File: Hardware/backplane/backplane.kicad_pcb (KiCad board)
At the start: 2 copper layers, 99.9 x 99.9 mm, 56 parts, among them J1 USB_B_Micro, SW1 SW_SPST, U2 MAX811SEUS-T, U3 MAX811SEUS-T, U4 PAL24, X1 CXO_DIP8

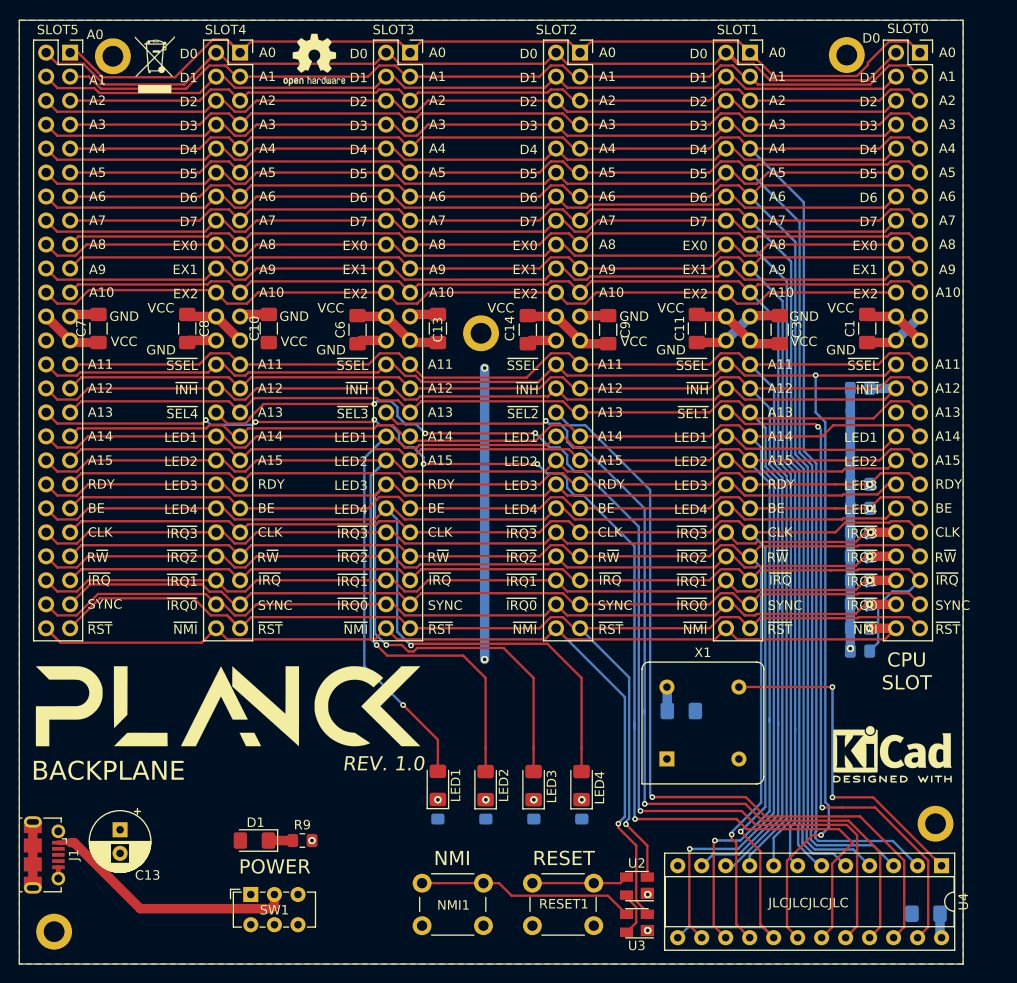
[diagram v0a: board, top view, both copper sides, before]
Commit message: Each slot has an individual interrupt line, to prevent two cards using the same interrupt line.
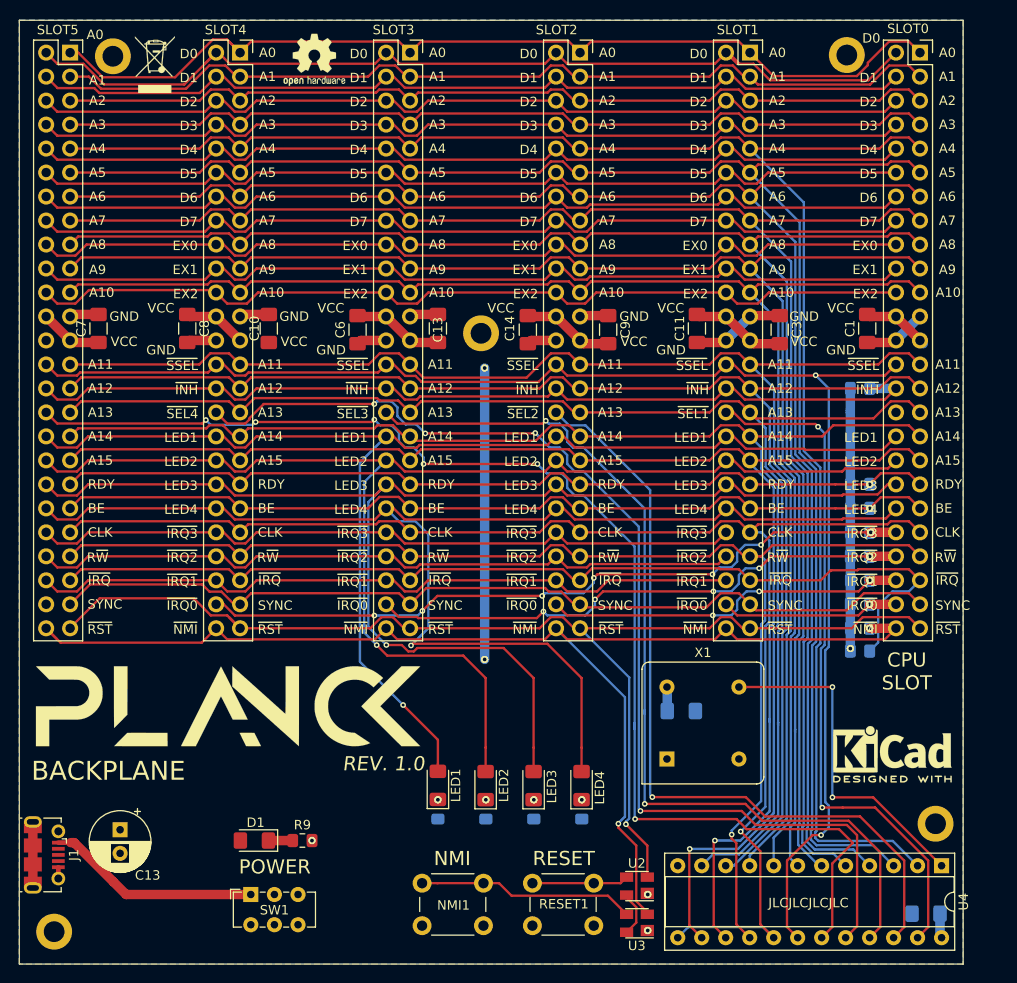
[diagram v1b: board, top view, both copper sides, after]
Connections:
- C13 pad 1: GND -> +5V
- C13 pad 2: +5V -> GND
- R3 pad 2: IRQ3 -> ~SLOT4_IRQ~
- R4 pad 2: IRQ2 -> ~SLOT3_IRQ~
- R5 pad 2: IRQ1 -> ~SLOT2_IRQ~
- R6 pad 2: IRQ0 -> ~SLOT1_IRQ~
- SLOT0 pad 42: IRQ3 -> ~SLOT4_IRQ~
- SLOT0 pad 44: IRQ2 -> ~SLOT3_IRQ~
- SLOT0 pad 46: IRQ1 -> ~SLOT2_IRQ~
- SLOT0 pad 48: IRQ0 -> ~SLOT1_IRQ~
- SLOT1 pad 42: IRQ3 -> EX3
- SLOT1 pad 44: IRQ2 -> EX4
- SLOT1 pad 46: IRQ1 -> EX5
- SLOT1 pad 48: IRQ0 -> ~SLOT1_IRQ~
- SLOT2 pad 42: IRQ3 -> EX3
- SLOT2 pad 44: IRQ2 -> EX4
- SLOT2 pad 46: IRQ1 -> EX5
- SLOT2 pad 48: IRQ0 -> ~SLOT2_IRQ~
- SLOT3 pad 42: IRQ3 -> EX3
- SLOT3 pad 44: IRQ2 -> EX4
- SLOT3 pad 46: IRQ1 -> EX5
- SLOT3 pad 48: IRQ0 -> ~SLOT3_IRQ~
- SLOT4 pad 42: IRQ3 -> EX3
- SLOT4 pad 44: IRQ2 -> EX4
- SLOT4 pad 46: IRQ1 -> EX5
- SLOT4 pad 48: IRQ0 -> ~SLOT4_IRQ~
- SLOT5 pad 42: IRQ3 -> EX3
- SLOT5 pad 44: IRQ2 -> EX4
- SLOT5 pad 46: IRQ1 -> EX5
- SLOT5 pad 48: IRQ0 -> Net-(SLOT5-Pad48)
- SW1 pad 1: +5V -> Net-(J1-Pad1)
- SW1 pad 2: Net-(J1-Pad1) -> +5V
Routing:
- net IRQ0: track 95.8 -> 0.00 mm, vias 1 -> 0
- net IRQ1: track 94.9 -> 0.00 mm, vias 1 -> 0
- net IRQ2: track 94.9 -> 0.00 mm, vias 1 -> 0
- net IRQ3: track 94.9 -> 0.00 mm, vias 1 -> 0
- net ~SLOT4_IRQ~: track 0.00 -> 77.8 mm, vias 0 -> 7
- net EX4: track 0.00 -> 76.7 mm
- net EX5: track 0.00 -> 75.9 mm
- net EX3: track 0.00 -> 75.9 mm
- net ~SLOT3_IRQ~: track 0.00 -> 59.9 mm, vias 0 -> 5
- net ~SLOT2_IRQ~: track 0.00 -> 39.0 mm, vias 0 -> 3
- net ~SLOT1_IRQ~: track 0.00 -> 19.8 mm, vias 0 -> 1
- net Net-(J1-Pad1): track 27.8 -> 23.4 mm
- net LED4: track 140.0 -> 142.6 mm
- net SYNC: track 95.6 -> 96.9 mm
- net CLK: track 152.1 -> 153.1 mm
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
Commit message: Update pin names
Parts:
- added R15: 1k, Resistor_SMD:R_0805_2012Metric_Pad1.15x1.40mm_HandSolder, F.Cu at (84.5, 36.4)
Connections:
- net IRQ renamed ~IRQ~
- net NMI renamed ~NMI~
- net ~SLOT1_IRQ~ renamed ~IRQ1~
- net ~SLOT2_IRQ~ renamed ~IRQ2~
- net ~SLOT3_IRQ~ renamed ~IRQ3~
- net ~SLOT4_IRQ~ renamed ~IRQ4~
- U4 pad 17: CLK -> Net-(U4-Pad17)
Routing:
- net LED4: track 142.6 -> 134.1 mm
- net LED3: track 140.7 -> 134.6 mm
- net CLK: track 153.1 -> 147.1 mm
- net LED2: track 138.8 -> 134.1 mm
- net +5V: track 118.5 -> 122.1 mm, vias 3 -> 4
- net ~SSEL~: track 158.7 -> 159.6 mm
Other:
- board text added: "EX3"
- board text added: "EX4"
- board text added: "EX5"
- board text added: "~IRQ4~"
- board text removed: "~IRQ0~"

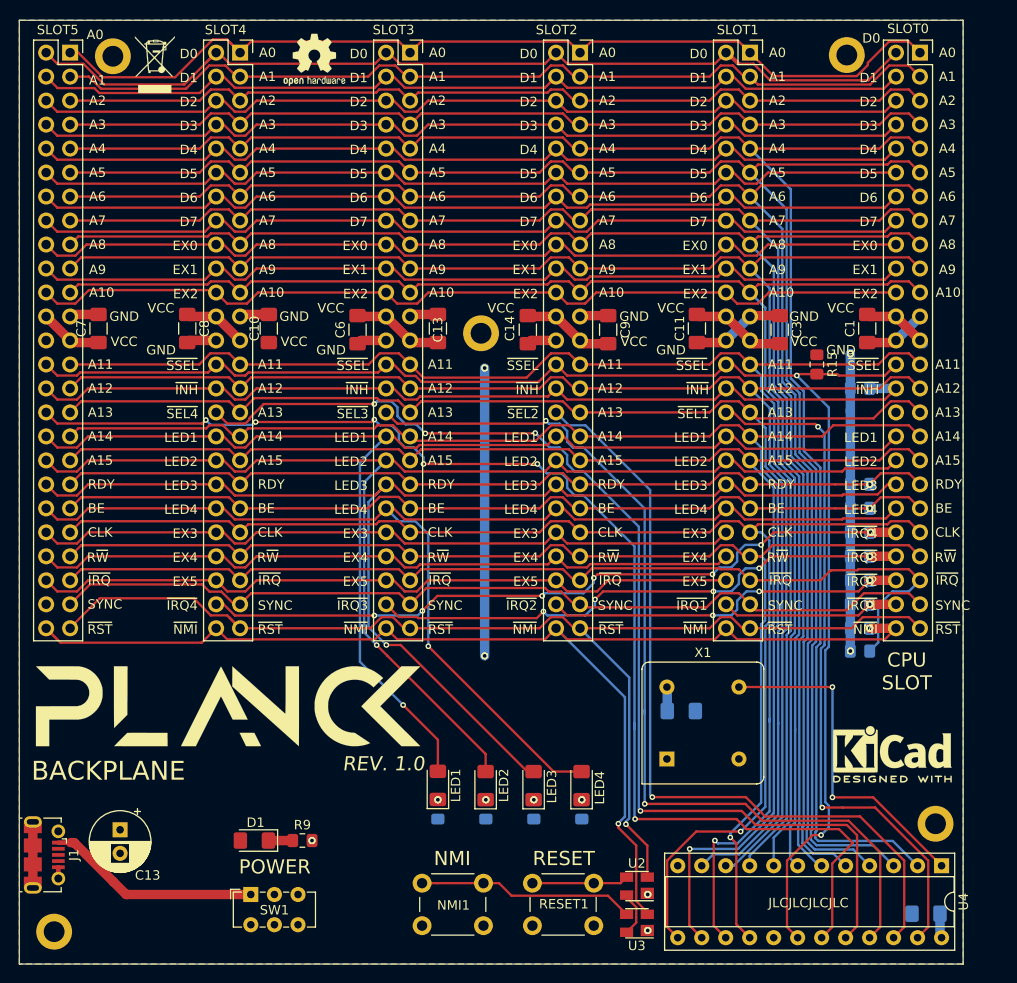
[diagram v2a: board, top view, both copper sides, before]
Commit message: rounded corners
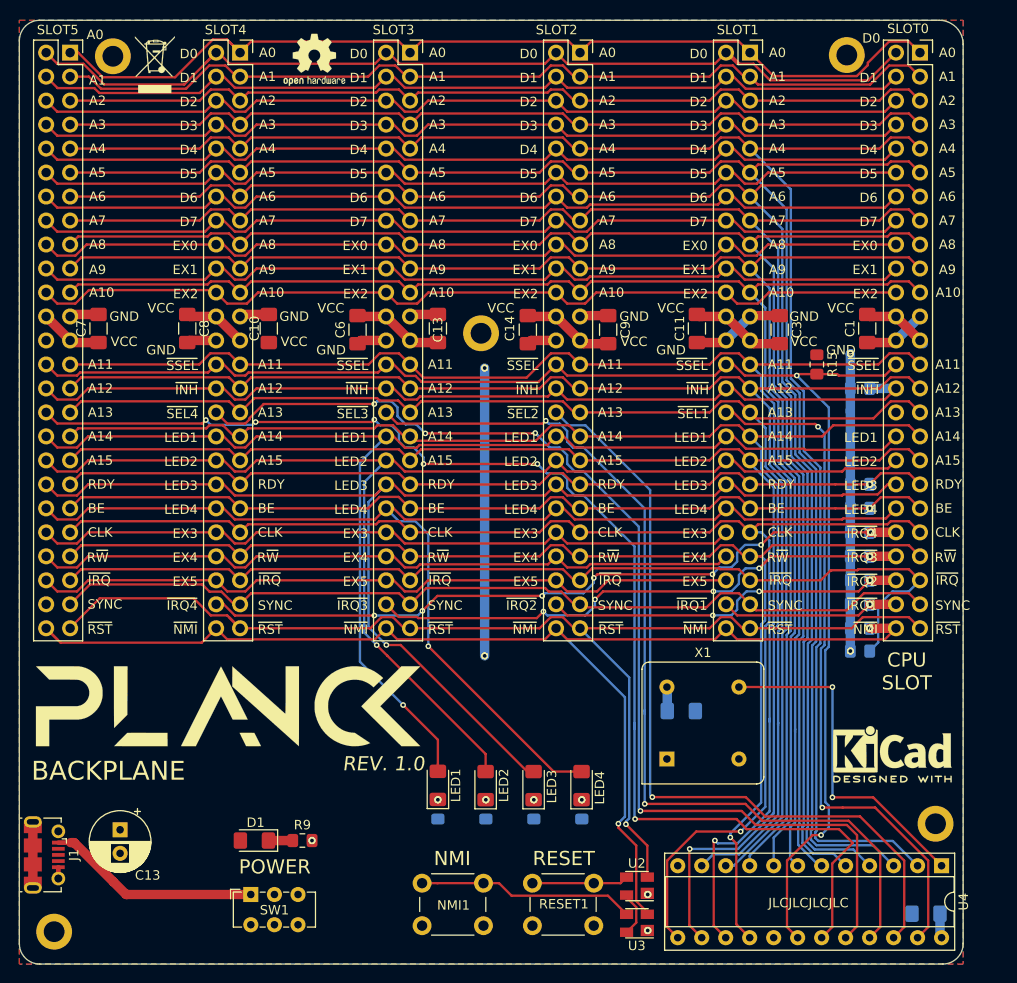
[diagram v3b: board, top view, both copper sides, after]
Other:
- outline, holes or cut-outs redrawn

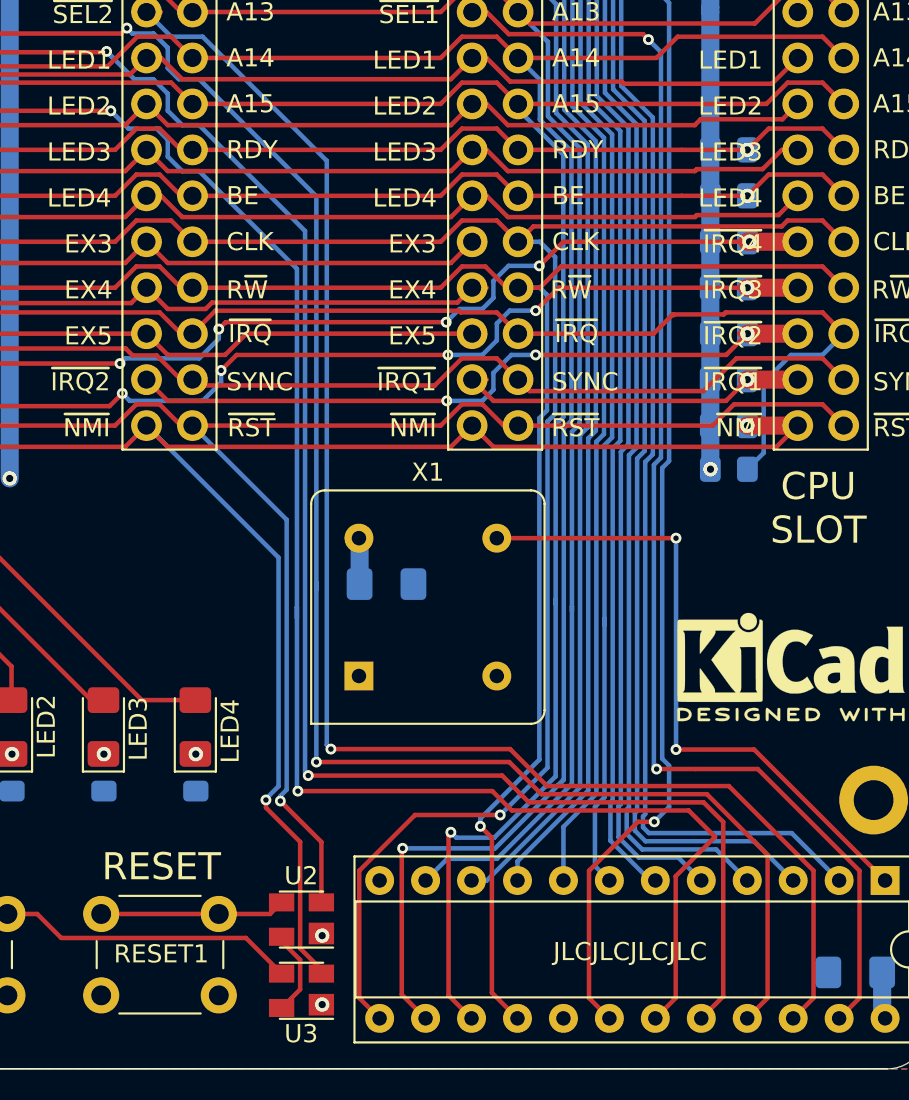
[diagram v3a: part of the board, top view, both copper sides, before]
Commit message: Add resistor between output of NMI MAX811 and NMI line to enable NMI to be controlled from the bus
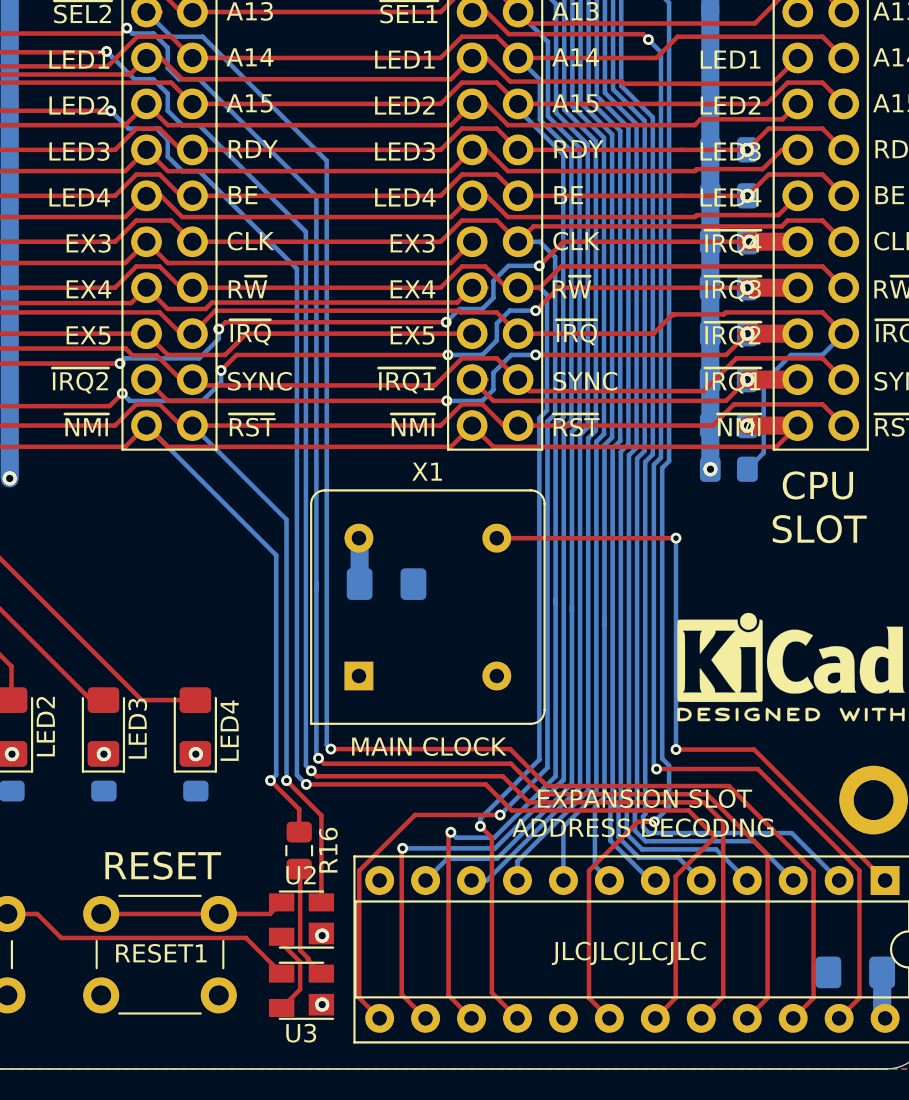
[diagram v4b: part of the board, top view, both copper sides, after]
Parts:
- added R16: 4.7k, Resistor_SMD:R_0805_2012Metric_Pad1.15x1.40mm_HandSolder, F.Cu at (65.3, 87.9)
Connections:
- U3 pad 2: ~NMI~ -> Net-(R16-Pad2)
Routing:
- net ~NMI~: track 134.5 -> 125.8 mm
- net Net-(R16-Pad2): track 0.00 -> 6.83 mm
- net SLOT5: track 135.5 -> 134.4 mm
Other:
- board text added: "EXPANSION SLOT ADDRESS DECODING"
- board text added: "MAIN CLOCK"

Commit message: Add backplane gerbers
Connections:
- U4 pad 13: CLK -> Net-(U4-Pad13)
- U4 pad 17: Net-(U4-Pad17) -> CLK
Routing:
- net CLK: track 147.1 -> 142.1 mm
- net ~IRQ4~: track 77.8 -> 81.4 mm
- net LED4: track 134.1 -> 136.0 mm

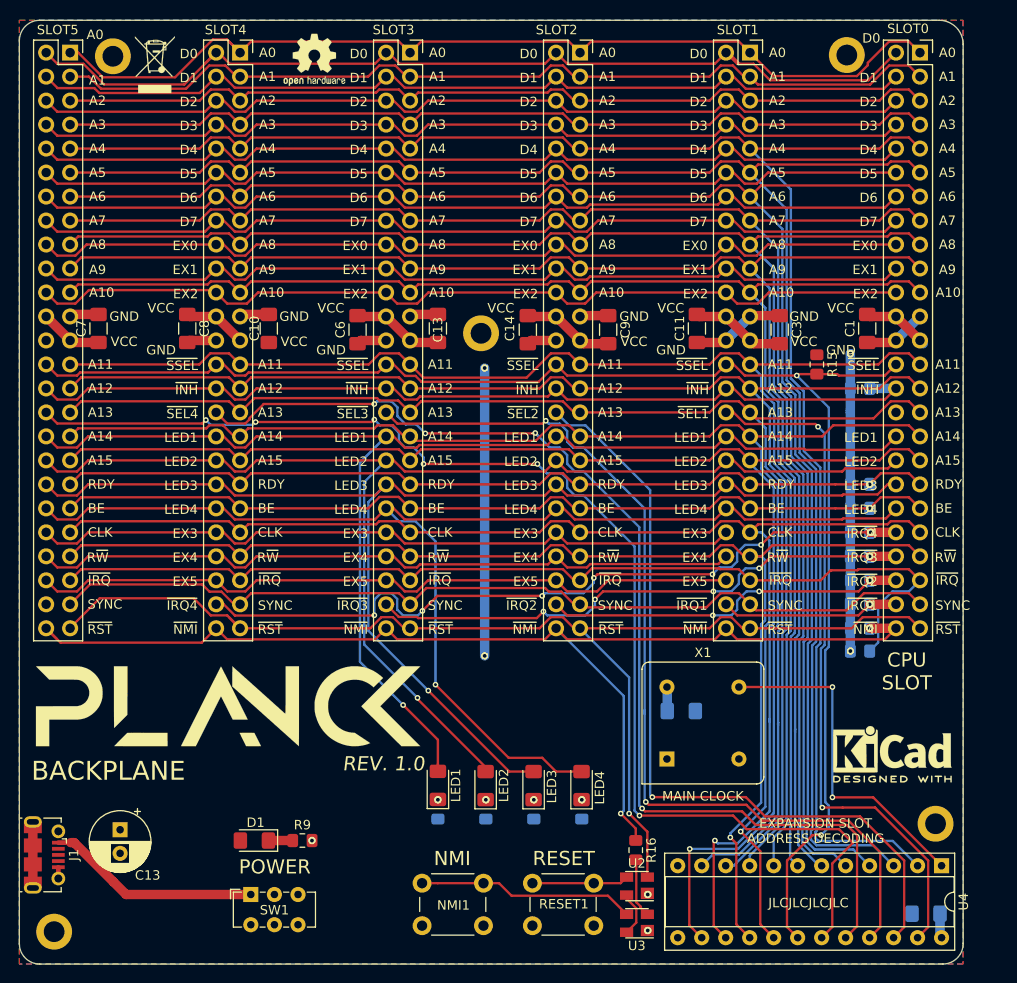
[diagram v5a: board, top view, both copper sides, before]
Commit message: Add clock stretching with counter and slow clock request from peripherals.
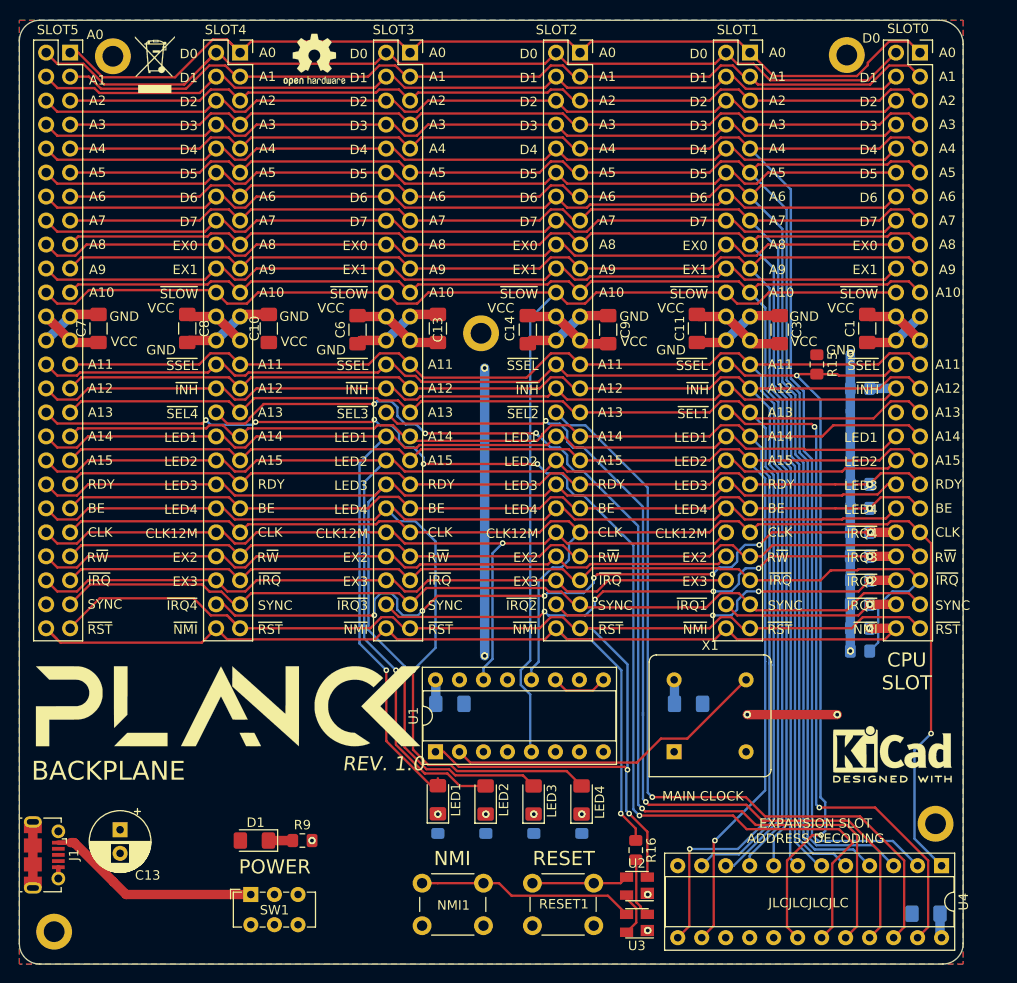
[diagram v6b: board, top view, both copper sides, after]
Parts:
- added C2: C_Small, Capacitor_SMD:C_1206_3216Metric_Pad1.42x1.75mm_HandSolder, B.Cu at (45.6, 72.4)
- added U1: 74HC161, Package_DIP:DIP-16_W7.62mm_Socket, F.Cu at (44.1, 77.5)
- X1: value CXO_DIP8 -> 24MHz
- moved LED1 1.52 mm to (44.3, 82.5)
- moved LED2 1.52 mm to (49.4, 82.6)
- moved LED3 1.52 mm to (54.5, 82.6)
- moved LED4 1.52 mm to (59.5, 82.6)
- moved R10 1.52 mm to (44.3, 85.1)
- moved R11 1.52 mm to (49.4, 85.1)
- moved R12 1.52 mm to (54.5, 85.1)
- moved R13 1.52 mm to (59.6, 85.1)
- moved C4 1.08 mm to (70.9, 72.4)
- moved X1 1.08 mm to (69.3, 77.5)
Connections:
- SLOT0 pad 22: EX2 -> ~SLOW~
- SLOT1 pad 22: EX2 -> ~SLOW~
- SLOT1 pad 42: EX3 -> CLK_12M
- SLOT1 pad 44: EX4 -> EX2
- SLOT1 pad 46: EX5 -> EX3
- SLOT2 pad 22: EX2 -> ~SLOW~
- SLOT2 pad 42: EX3 -> CLK_12M
- SLOT2 pad 44: EX4 -> EX2
- SLOT2 pad 46: EX5 -> EX3
- SLOT3 pad 22: EX2 -> ~SLOW~
- SLOT3 pad 42: EX3 -> CLK_12M
- SLOT3 pad 44: EX4 -> EX2
- SLOT3 pad 46: EX5 -> EX3
- SLOT4 pad 22: EX2 -> ~SLOW~
- SLOT4 pad 42: EX3 -> CLK_12M
- SLOT4 pad 44: EX4 -> EX2
- SLOT4 pad 46: EX5 -> EX3
- SLOT5 pad 22: EX2 -> ~SLOW~
- SLOT5 pad 42: EX3 -> CLK_12M
- SLOT5 pad 44: EX4 -> EX2
- SLOT5 pad 46: EX5 -> EX3
- U4 pad 1: Net-(U4-Pad1) -> CLK
- U4 pad 13: Net-(U4-Pad13) -> A14
- U4 pad 14: A14 -> A15
- U4 pad 15: A15 -> Net-(U4-Pad15)
- U4 pad 16: R~W~ -> Net-(U4-Pad16)
- U4 pad 17: CLK -> Net-(U4-Pad17)
- X1 pad 5: Net-(U4-Pad1) -> /CLK_24M
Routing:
- net ~SLOW~: track 0.00 -> 145.7 mm
- net CLK_12M: track 0.00 -> 91.2 mm, vias 0 -> 1
- net EX4: track 76.7 -> 0.00 mm
- net EX5: track 75.9 -> 0.00 mm
- net R~W~: track 139.0 -> 94.9 mm, vias 1 -> 0
- net Net-(U4-Pad1): track 36.1 -> 0.00 mm, vias 2 -> 0
- net /CLK_24M: track 0.00 -> 34.5 mm
- net GND: track 46.3 -> 70.1 mm, vias 3 -> 5
- net ~RESET~: track 126.8 -> 148.8 mm, vias 1 -> 2
- net EX2: track 95.1 -> 76.7 mm
- net CLK: track 142.1 -> 150.9 mm
- net LED4: track 136.0 -> 144.0 mm
- net Net-(U1-Pad11): track 0.00 -> 6.01 mm
- net LED3: track 134.8 -> 140.4 mm
- net LED2: track 134.1 -> 139.1 mm
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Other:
- board text added: "CLK12M"
- board text added: "~SLOW~"
- board text removed: "EX4"
- board text removed: "EX5"
